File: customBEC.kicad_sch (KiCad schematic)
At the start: 19 parts, among them J18 ESC Logic Power, J19 Flight Controller Power, J3 From BEC, J4 From Battery, U4 TPS5430DDA

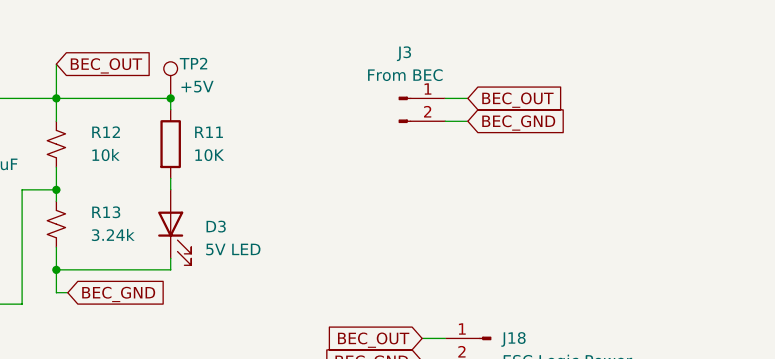
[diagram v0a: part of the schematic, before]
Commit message: Made Board Traces Cleaner
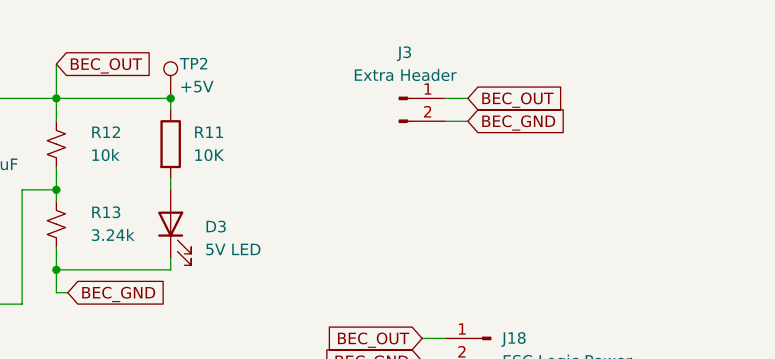
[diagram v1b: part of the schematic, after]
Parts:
- J3: value From BEC -> Extra Header
- J4: footprint Connector_PinHeader_2.54mm:PinHeader_1x02_P2.54mm_Vertical -> Connector_Hirose:Hirose_DF13-02P-1.25DS_1x02_P1.25mm_Horizontal
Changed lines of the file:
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@@
 			)
 		)
-		(property "Footprint" "Connector_PinHeader_2.54mm:PinHeader_1x02_P2.54mm_Vertical"
+		(property "Footprint" "Connector_Hirose:Hirose_DF13-02P-1.25DS_1x02_P1.25mm_Horizontal"
 			(at 46.99 33.02 0)
 			(effects
@@
 			)
 		)
-		(property "Value" "From BEC"
+		(property "Value" "Extra Header"
 			(at 215.265 30.48 0)
 			(effects

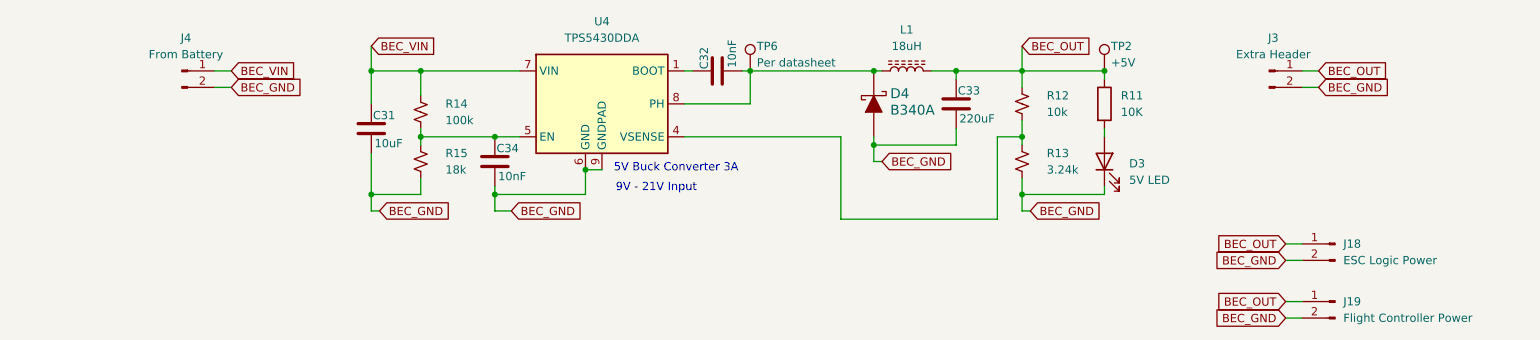
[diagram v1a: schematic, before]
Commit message: re-annotate and fix drc issues
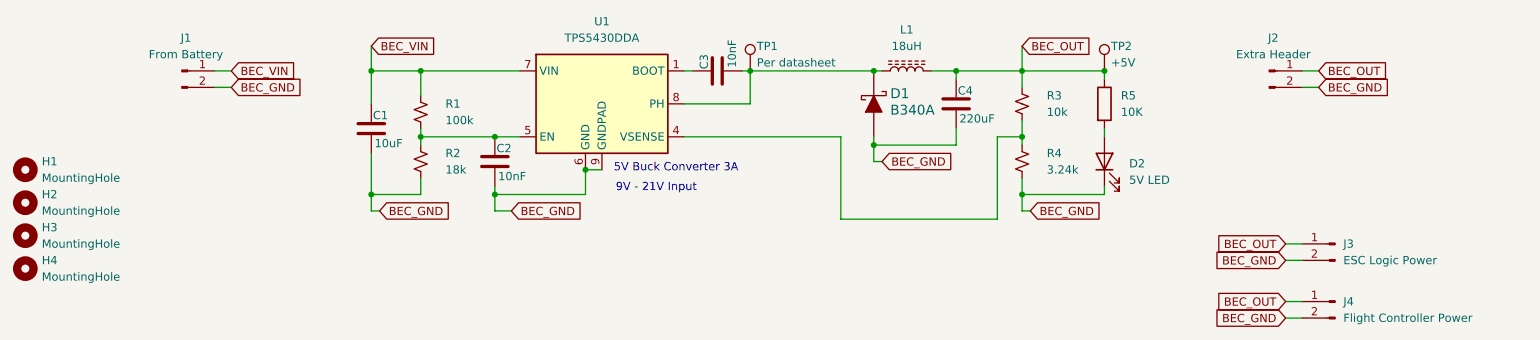
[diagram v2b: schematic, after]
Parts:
- added H1, H2, H3, H4: MountingHole, MountingHole:MountingHole_3.2mm_M3, symbol Mechanical:MountingHole
- renumbered C31 to C1, C34 to C2, C32 to C3, C33 to C4, D4 to D1, D3 to D2, J4 to J1, J3 to J2, J18 to J3, J19 to J4, R14 to R1, R15 to R2, R12 to R3, R13 to R4, R11 to R5, TP6 to TP1, U4 to U1
